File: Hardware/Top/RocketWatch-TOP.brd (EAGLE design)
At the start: 38 x 38 mm, 52 parts, among them SW1 SWITCH.MOM, SW2 SWITCH.MOM, SW5 SWITCH.MOM, U2 NRF52832_MODULE_MDBT42, U4 PCF8523

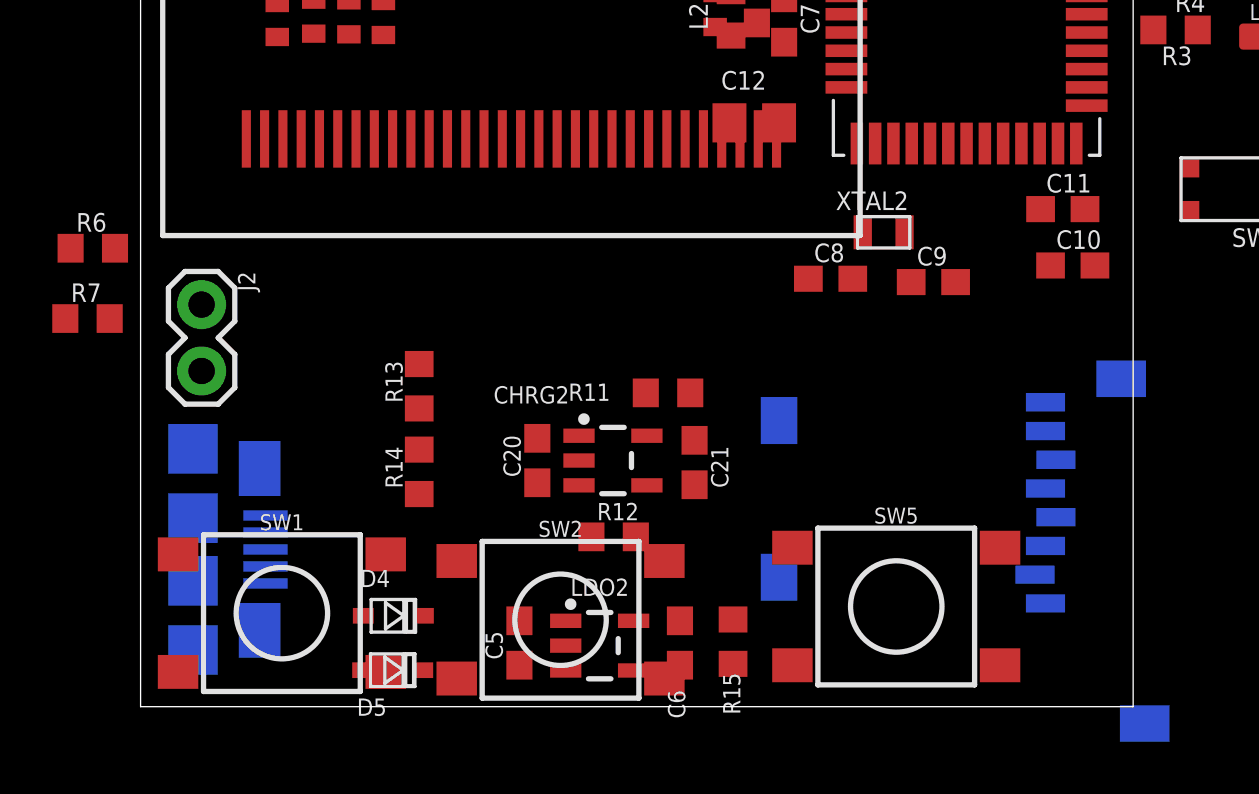
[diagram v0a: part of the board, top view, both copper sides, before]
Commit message: finished top schematic and  board according to take 001 video
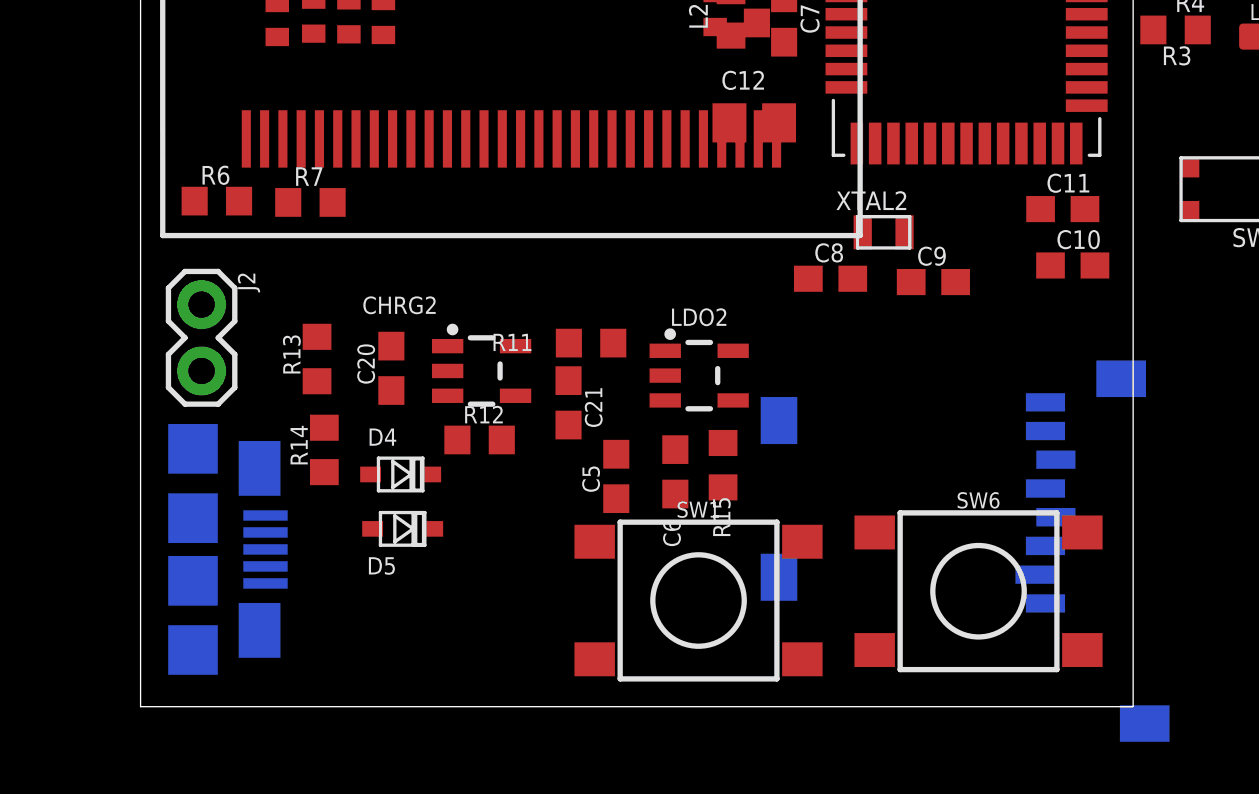
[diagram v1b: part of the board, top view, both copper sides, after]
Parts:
- removed SW2, SW5: SWITCH.MOM, LinnesLab-Switches:TACTILE_SWITCH_SMD_6.2MM_TALL
- added SW6: SWITCH.MOM, LinnesLab-Switches:TACTILE_SWITCH_SMD_6.2MM_TALL
- moved SW1 16.0 mm to (21.4, 4.06)
- moved LDO2 11.0 mm to (21.4, 12.7)
- moved R7 9.62 mm to (6.50, 19.3)
- moved C5 7.38 mm to (18.2, 8.81)
- moved R15 6.77 mm to (22.3, 9.25)
- moved C20 6.61 mm to (9.60, 13.0)
- moved C6 6.56 mm to (20.5, 8.99)
- moved R12 6.33 mm to (13.0, 10.2)
- moved CHRG2 6.09 mm to (13.1, 12.9)
- moved D5 5.42 mm to (10.0, 6.81)
- moved D4 5.42 mm to (9.96, 8.89)
- moved C21 5.34 mm to (16.4, 11.6)
- moved R6 5.08 mm to (2.92, 19.4)
- moved R13 4.05 mm to (6.76, 13.3)
- moved R14 3.73 mm to (7.04, 9.83)
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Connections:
- net VBATT renamed VBAT
- new net SW1: SW1.A1, SW6.A1
- net GND: now also SW1.B1, SW1.B2, SW6.B1, SW6.B2, USB2.S1, USB2.S2, USB2.S3, USB2.S4, USB2.S5, USB2.S6
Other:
- board text added: "Data to send to bottom board 3.3V GND I2C TIA 2-3x GPIO PPG (Pulse sensor output)"

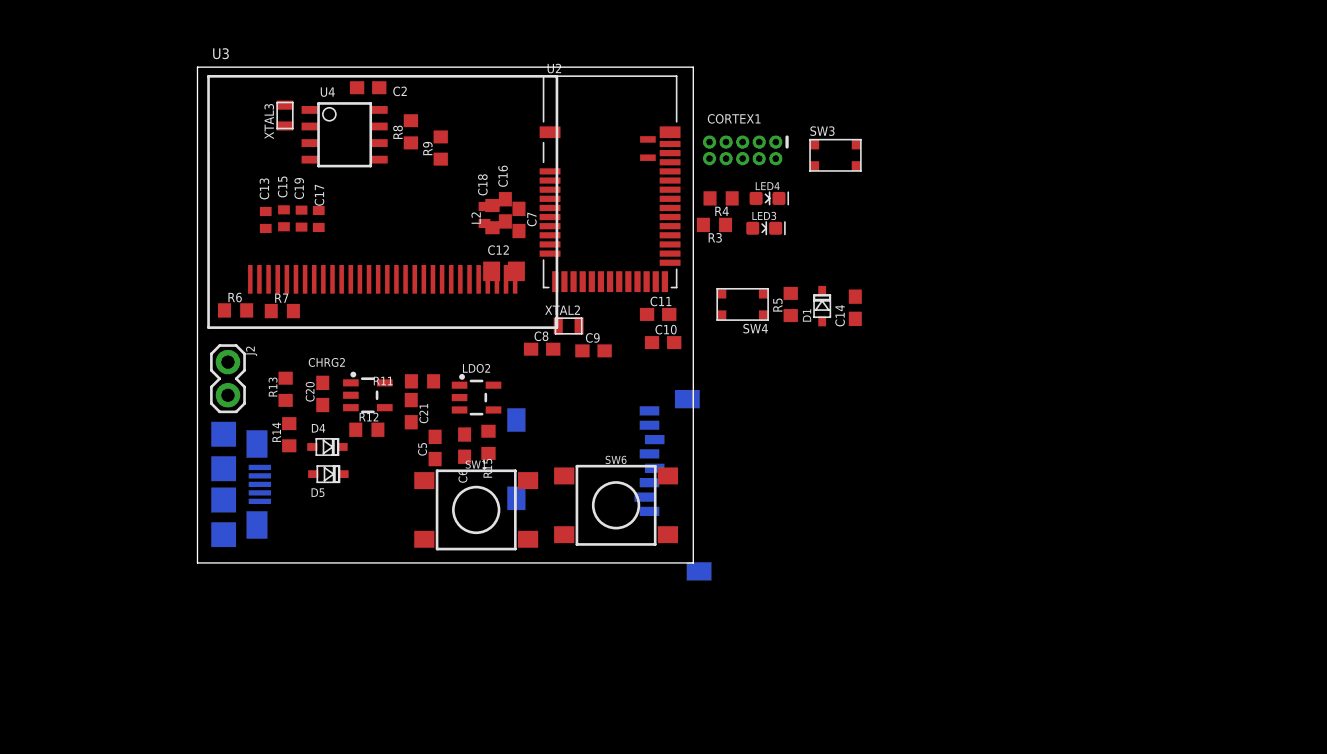
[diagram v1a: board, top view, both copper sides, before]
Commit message: changed schematic and board based on video take 002
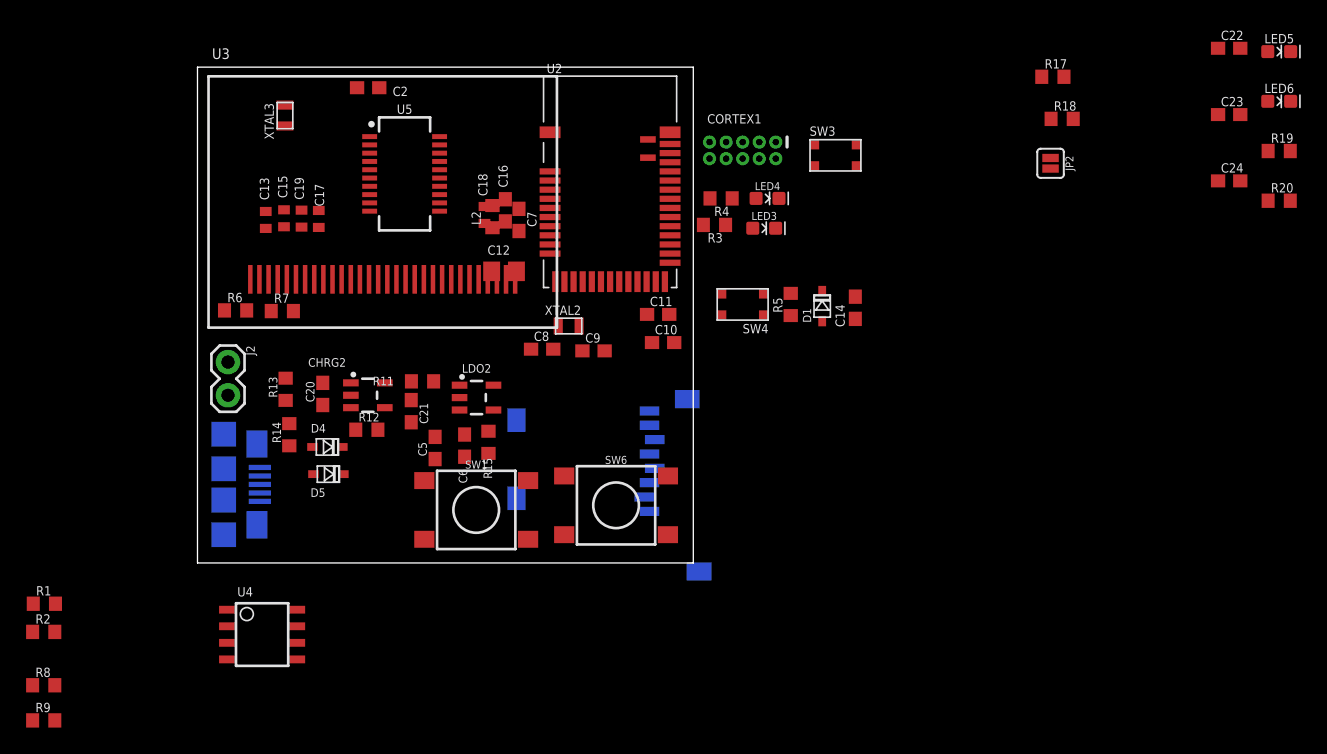
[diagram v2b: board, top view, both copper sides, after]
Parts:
- added C22: 100n, LinnesLab-Passives:C0603
- added C23, C24: 47p, LinnesLab-Passives:C0603
- added JP2: (no value), LinnesLab-Switches:SMT-JUMPER_2_NO_SILK
- added LED5: RED, LinnesLab-LED:LED-0603
- added LED6: YELLOW, LinnesLab-LED:LED-0603
- added R1, R2: 0, LinnesLab-Passives:R0603
- added R17, R18: 27, LinnesLab-Passives:R0603
- added R19, R20: 1k, LinnesLab-Passives:R0603
- added U5: FT231XS, LinnesLab-DigitalIC:SSOP20_L
- moved R9 53.4 mm to (-11.8, -12.1), turned to 0 degrees
- moved R8 50.9 mm to (-11.8, -9.37), turned to 0 degrees
- moved U4 38.8 mm to (4.95, -5.49)
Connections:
- new net !CTS: JP2.2, U5.9
- new net FT3V3: U5.13
- new net N$23: R17.2, U5.12
- new net N$24: R18.2, U5.11
- new net N$25: LED5.C, R19.2
- new net N$26: LED6.C, R20.2
- new net RXD.FT: R2.1
- new net RXD.NRF: R1.2, U2.21
- new net RXLED: R19.1, U5.17
- new net TXD.FT: R1.1
- new net TXD.NRF: R2.2, U2.19
- new net TXLED: R20.1, U5.10
- net 3.3V: now also C22.2, LED5.A, LED6.A, U5.14, U5.3
- net DTR: now also U5.1
- net GND: now also C22.1, C23.2, C24.1, JP2.1, U5.16, U5.6
- net RXD: now also U5.4; no longer U2.21
- net SCL: now also R9.1; no longer R8.1
- net SDA: now also R8.1; no longer R9.1
- net TXD: now also U5.20; no longer U2.19
- net USB+: now also C23.1, R18.1
- net USB-: now also C24.2, R17.1
- net V_USB: now also U5.15

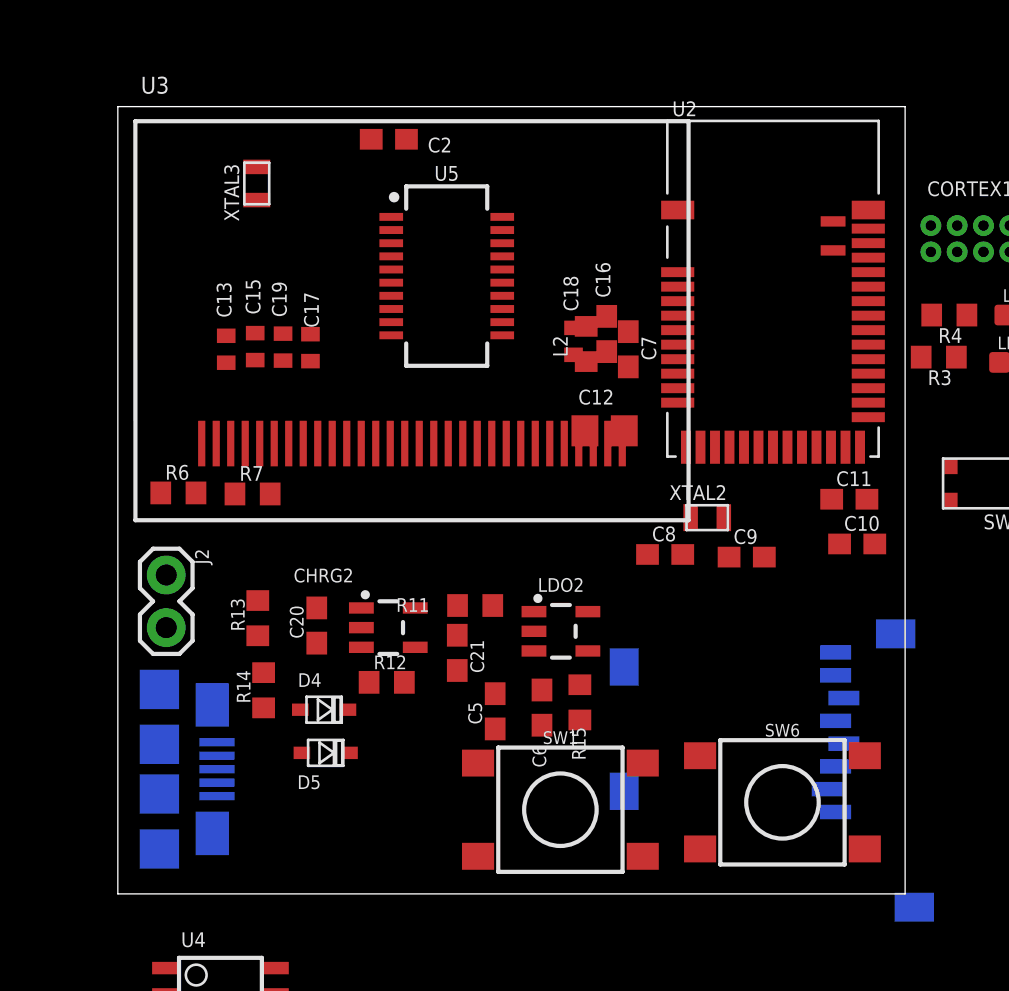
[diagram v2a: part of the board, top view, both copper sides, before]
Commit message: changes to top and bottom board based on take 002 video. Basic schematic and board is complete (no routing done yet)
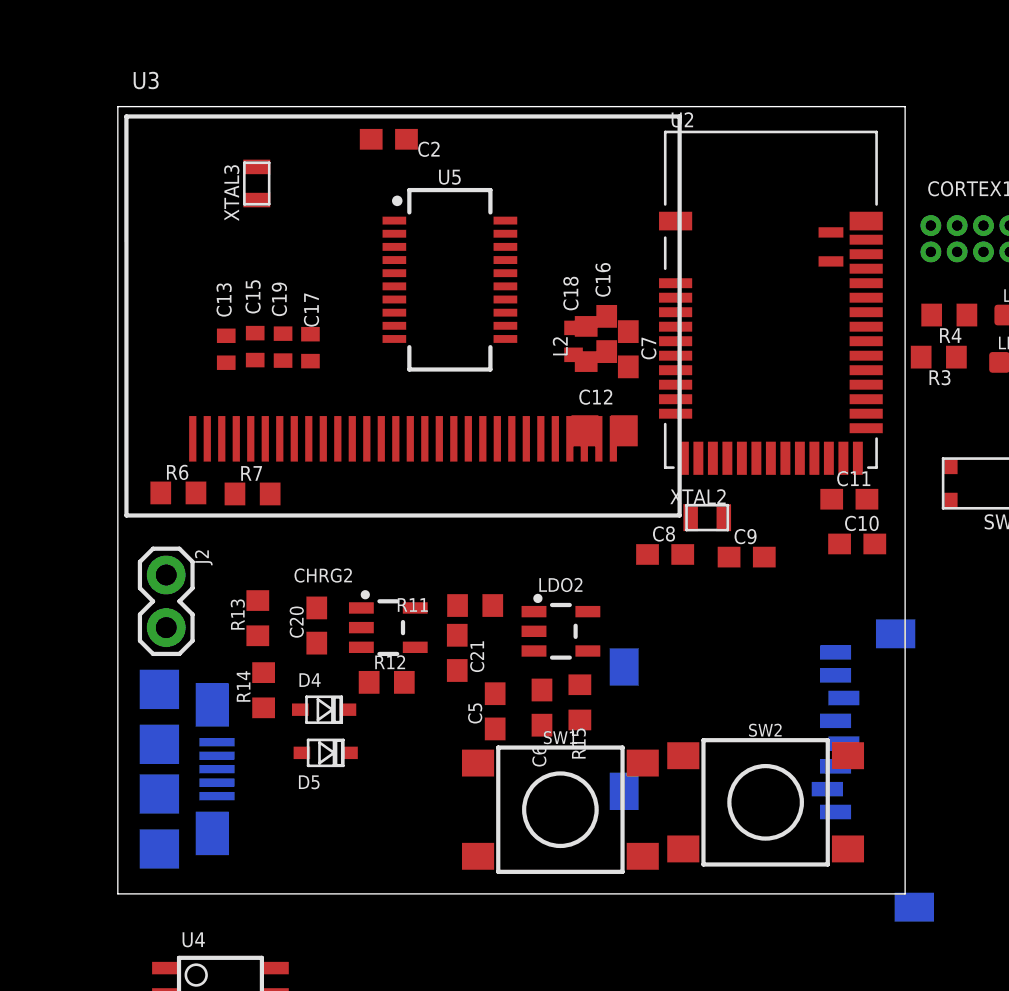
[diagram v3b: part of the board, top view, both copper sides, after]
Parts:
- removed SW6: SWITCH.MOM, LinnesLab-Switches:TACTILE_SWITCH_SMD_6.2MM_TALL
- added SW2: SWITCH.MOM, LinnesLab-Switches:TACTILE_SWITCH_SMD_6.2MM_TALL
- moved U2 0.54 mm to (31.5, 28.7)
- moved U3 0.49 mm to (13.8, 23.2)
- moved U5 0.23 mm to (16.0, 29.6)
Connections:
- removed net BATT: R13.1, R14.2
- removed net CD1: SD2.CD1
- removed net CHRG.STAT: CHRG2.1, R12.1
- removed net CS.OLED: U3.13
- removed net DC.OLED: U3.15
- removed net RESET.OLED: U3.14
- removed net SD.CS: SD2.2
- removed net SW1: SW1.A1, SW6.A1
- new net A4/BATT: R13.1, R14.2, U2.5
- new net A6/TIA: U2.7
- new net A7/PPG: U2.8
- new net D11/SW1: SW1.A1, U2.25
- new net D15/SW2: SW2.A1, U2.29
- new net D16/CS.OLED: U2.30, U3.13
- new net D27/CHRG.STATUS: CHRG2.1, R12.1, U2.4
- new net D29/LED.CTRL: U2.6
- new net D3/RESET.OLED: U2.17, U3.14
- new net D4/DC.OLED: U2.16, U3.15
- new net D5/CD1: SD2.CD1, U2.18
- new net D7/SD.CS: SD2.2, U2.20
- net GND: now also SW2.B1, SW2.B2; no longer SW6.B1, SW6.B2
